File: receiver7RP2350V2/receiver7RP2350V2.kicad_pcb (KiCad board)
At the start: 4 copper layers, 46.5 x 51.8 mm, 69 parts, among them J1 BM04B-SRSS-TB, J10 S2B-PH-SM4-TB, J4 2pads, J6 MM60-52B1-E1-R650, J7 USB4105-GF-A, J8 S2B-PH-SM4-TB, U1 RP2350_60QFN, U2 USBLC6-2SC6, U3 AP7361C-33Y5-13, U4 MCP73871-2CCI_ML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

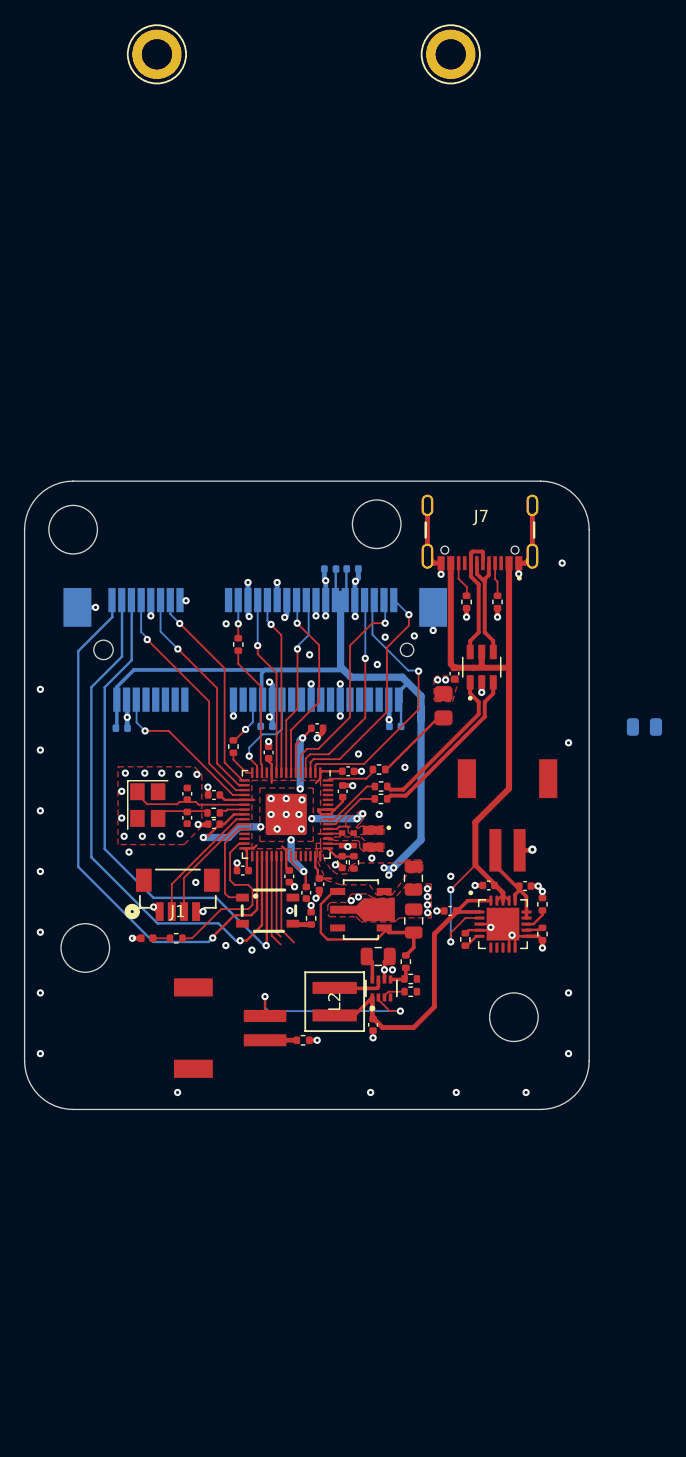
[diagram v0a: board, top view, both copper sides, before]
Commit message: add rp2350V2
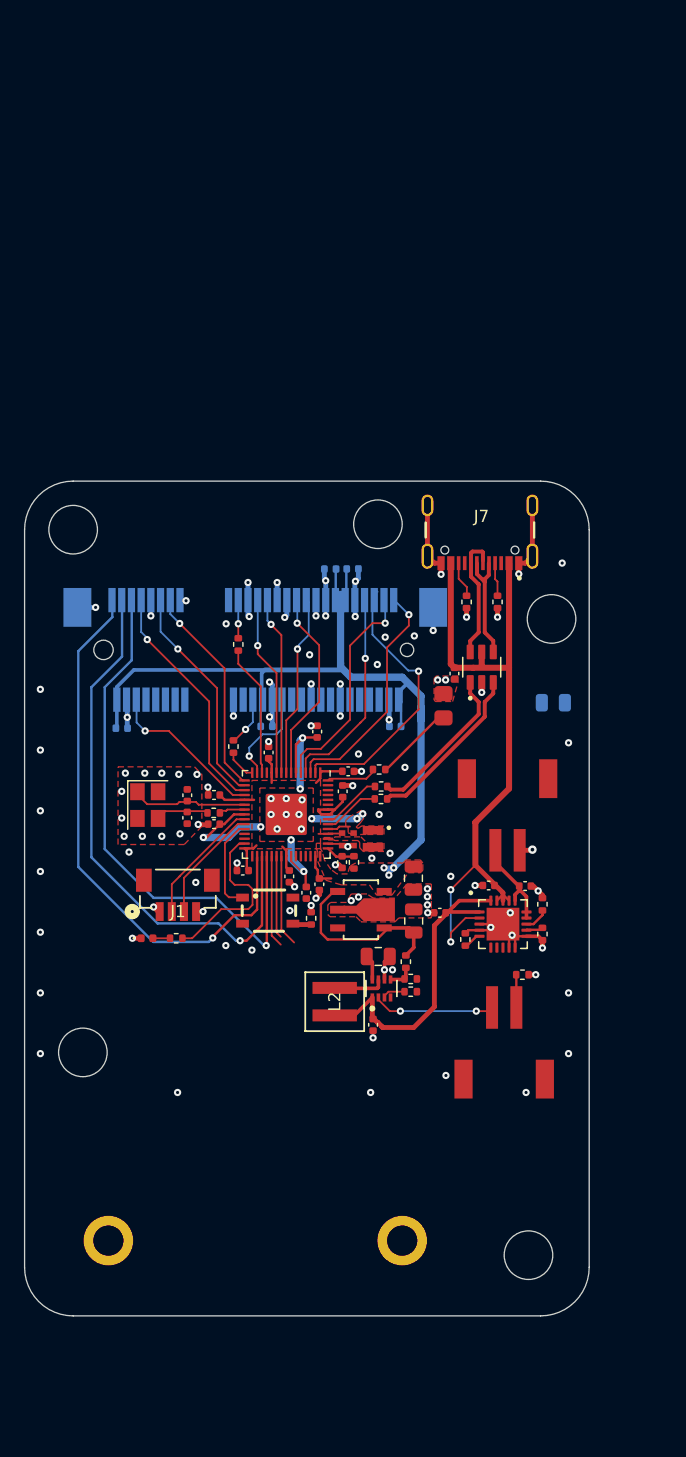
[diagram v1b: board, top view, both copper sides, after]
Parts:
- added H8: MountingHole, TF:MountingHole_4mm_t4, F.Cu at (116.6, 85.2)
- REF** (x2): moved to B.Cu
- moved REF** 101.7 mm to (94.4, 144.2), turned to 180 degrees
- moved REF** 99.8 mm to (118.6, 144.2), turned to 180 degrees
- moved J10 22.7 mm to (127.0, 128.0), turned to 0 degrees
- moved H6 19.6 mm to (129.0, 145.4)
- moved R15 18.9 mm to (128.5, 122.3)
- moved H8 16.4 mm to (130.9, 93.0)
- moved H5 8.60 mm to (92.3, 128.7)
- moved C19 7.76 mm to (131.1, 99.9)
- moved C27 0.86 mm to (121.7, 117.2)
- moved C11 0.28 mm to (111.6, 102.3), turned to 90 degrees
- moved C20 0.11 mm to (100.9, 107.5)
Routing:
- net Net-(U5-EN): track 16.4 -> 10.3 mm
- net /V_LOAD: track 25.2 -> 26.5 mm
- net GND: track 76.0 -> 75.3 mm, vias 112 -> 111
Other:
- board size 46.5 x 51.8 mm -> 46.5 x 68.8 mm

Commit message: add panelized files
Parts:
- removed C19, C29: 10u, Capacitor_SMD:C_0805_2012Metric
- removed H8 (x2): MountingHole, TF:MountingHole_4mm_t4
- removed L2: 1uH, EXLA1V0402_1RO_R:IND_EXLA-0402_EAT-L
- removed R17: 750k, Resistor_SMD:R_0402_1005Metric
- removed R18: 71.5k 1%, Resistor_SMD:R_0402_1005Metric
- removed REF** (x2): , NT4R1600:JAE_Electronics-NT4R1600-MFG
- removed U3: AP7361C-33Y5-13, AP7361C_33Y5_13:SOT89-5_DIO-M_MODGND
- added C30: 10u, Capacitor_SMD:C_0805_2012Metric, F.Cu at (129.7, 109.4)
- added D2: SMAJ6.0CA, Diode_SMD:D_SMA, F.Cu at (129.8, 102.0)
- added G***: LOGO, LOGO, F.Cu at (109.4, 141.8)
- added H1: MountingHole, MountingHole:MountingHole_2.5mm, F.Cu at (130.8, 94.1)
- added H5: MountingHole, MountingHole:MountingHole_2.7mm_M2.5_Pad_Via, F.Cu at (116.7, 85.6)
- added J2: NT4R1600, NT4R1600:JAE_Electronics-NT4R1600-MFG, B.Cu at (94.4, 144.2)
- added J3: NT4R1600, NT4R1600:JAE_Electronics-NT4R1600-MFG, B.Cu at (118.6, 144.2)
- added J5: USB4105-GF-A, USB4105_GF_A:GCT_USB4105-GF-A, F.Cu at (105.5, 83.7)
- added R19: 3.3k, Resistor_SMD:R_0402_1005Metric, F.Cu at (121.5, 113.4)
- added R20: 330k, Resistor_SMD:R_0402_1005Metric, F.Cu at (124.4, 107.3)
- C22, C23: value 10u -> 4.7u; footprint Capacitor_SMD:C_0805_2012Metric -> Capacitor_SMD:C_0402_1005Metric
- C24: moved to B.Cu
- C25: value 10u -> 100n
- C26: footprint Capacitor_SMD:C_0402_1005Metric -> Capacitor_SMD:C_0805_2012Metric
- C27, C28: value 10u -> 4.7u
- H2: renamed from H5; footprint TF:MountingHole_4mm_t4 -> MountingHole:MountingHole_2.7mm_M2.5_Pad_Via
- H3: renamed from H6; footprint TF:MountingHole_4mm_t4 -> MountingHole:MountingHole_2.7mm_M2.5_Pad_Via
- H4: renamed from H7; footprint TF:MountingHole_4mm_t4 -> MountingHole:MountingHole_2.7mm_M2.5_Pad_Via
- R12: value 3.3k -> 10k
- R14: value 24.9k -> 3.3k
- R15, R16: value 3.3k -> 5.1k
- U4: value MCP73871-2CCI_ML -> MP2664GG-0000-Z; footprint MCP73871_2CCI_ML:QFN50P400X400X100-21N -> MP2664GG-0000-Z:QFN50P200X200X105-10N
- U5: value TPS610333DRLR -> NCP186AMX330TAG; footprint TPS61033DRLR:DRL0008A-MFG_mod2 -> NCP186AMX330TAG:PSON40P160X120X45-9N
- moved R16 41.9 mm to (99.5, 86.8), turned to -90 degrees
- moved R15 39.4 mm to (111.5, 86.8), turned to 90 degrees
- moved J10 36.3 mm to (92.0, 118.2)
- moved H2 25.0 mm to (94.4, 153.6)
- moved R13 14.0 mm to (126.0, 105.5)
- moved H3 13.2 mm to (118.6, 153.6)
- moved R12 11.8 mm to (124.4, 106.2), turned to 180 degrees
- moved R14 11.6 mm to (121.0, 111.9), turned to -90 degrees
- moved C28 11.0 mm to (116.2, 115.4), turned to 180 degrees
- moved J8 9.20 mm to (127.2, 118.3), turned to 0 degrees
- moved C26 8.45 mm to (128.9, 106.5)
- moved U4 8.23 mm to (126.9, 109.9), turned to -90 degrees
- moved C27 7.53 mm to (127.5, 112.4)
- moved U5 6.63 mm to (117.5, 116.8), turned to -90 degrees
- moved C25 6.20 mm to (124.8, 108.8), turned to -90 degrees
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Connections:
- C22 pad 1: GND -> +3V3
- C22 pad 2: +3V3 -> GND
- C23 pad 1: +5V -> /V_LOAD
- C24 pad 1: VBUS -> /VPHONE
- C25 pad 1: VBUS -> /VDD
- C26 pad 1: Net-(U4-VBAT) -> /VBUS
- C27 pad 1: /V_LOAD -> /BAT_PWR
- C28 pad 1: GND -> +3V3
- C28 pad 2: /V_LOAD -> GND
- J10 pad 1: Net-(U5-EN) -> /V_LOAD
- J10 pad 2: Net-(J10-Pad2) -> /V_EN
- J7 pad A4_B9: VBUS -> /VPHONE
- J7 pad B4_A9: VBUS -> /VPHONE
- J8 pad 2: Net-(U4-VBAT) -> /BAT_PWR
- R12 pad 1: GND -> Net-(U4-NTC)
- R12 pad 2: Net-(U4-PROG1) -> /VDD
- R13 pad 2: Net-(U4-THERM) -> Net-(U4-NTC)
- R14 pad 1: GND -> /SCL0
- R14 pad 2: Net-(U4-PROG3) -> +3V3
- R15 pad 2: Net-(J10-Pad2) -> Net-(J5-CC1)
- R16 pad 1: GND -> Net-(J5-CC2)
- R16 pad 2: Net-(U5-MODE) -> GND
- S1 pad 3: Net-(R1-Pad2) -> unconnected-(S1-Pad3)
- U1 pad 35: /GPIO23 -> /INT_BAT
- U1 pad 36: unconnected-(U1-GPIO24-Pad36) -> /SDA0
- U1 pad 37: unconnected-(U1-GPIO25-Pad37) -> /SCL0
- U2 pad 5: VBUS -> /VPHONE
- U4 pad 1: /V_LOAD -> /VBUS
- U4 pad 10: GND -> /V_LOAD
- U4 pad 2: VBUS -> Net-(U4-NTC)
- U4 pad 3: GND -> /INT_BAT
- U4 pad 4: GND -> /VDD
- U4 pad 5: Net-(U4-THERM) -> GND
- U4 pad 6: unconnected-(U4-~{PG}-Pad6) -> /SCL0
- U4 pad 7: unconnected-(U4-STAT2-Pad7) -> /SDA0
- U4 pad 8: unconnected-(U4-STAT1/*LBO-Pad8) -> /BAT_PWR
- U4 pad 9: GND -> /BAT_PWR
- U5 pad 1: /V_LOAD -> +3V3
- U5 pad 2: Net-(U5-EN) -> +3V3
- U5 pad 3: Net-(U5-MODE) -> GND
- U5 pad 4: unconnected-(U5-PG-Pad4) -> +3V3
- U5 pad 5: Net-(U5-FB) -> GND
- U5 pad 6: GND -> /V_EN
- U5 pad 7: Net-(U5-SW) -> /V_LOAD
- U5 pad 8: +5V -> /V_LOAD
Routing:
- net VBUS: track 57.0 -> 0.00 mm, vias 2 -> 0
- net /VBUS: track 0.00 -> 43.8 mm
- net /INT_BAT: track 0.00 -> 42.2 mm, vias 0 -> 2
- net /V_EN: track 0.00 -> 35.7 mm
- net /SDA0: track 0.00 -> 33.8 mm, vias 0 -> 2
- net /V_LOAD: track 26.5 -> 59.9 mm
- net /SCL0: track 0.00 -> 32.4 mm, vias 0 -> 2
- net /VPHONE: track 0.00 -> 20.6 mm, vias 0 -> 2
- net +5V: track 17.4 -> 0.00 mm
- net GND: track 75.3 -> 60.1 mm, vias 111 -> 180
- net Net-(U5-EN): track 10.3 -> 0.00 mm, vias 2 -> 0
- net Net-(U4-VBAT): track 7.68 -> 0.00 mm
- net /GPIO23: track 7.60 -> 0.00 mm
- net unconnected-(U1-GPIO25-Pad37): track 7.55 -> 0.00 mm
- net unconnected-(U1-GPIO24-Pad36): track 6.78 -> 0.00 mm
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- added copper zone on F.Cu, net /BAT_PWR
- added copper zone on F.Cu, net /VBUS
- added copper zone on F.Cu, net /VDD
- added copper zone on F.Cu, net /V_LOAD
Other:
- board size 46.5 x 68.8 mm -> 46.5 x 78.3 mm
- rule pad_to_mask_clearance: 0.0508 -> 0

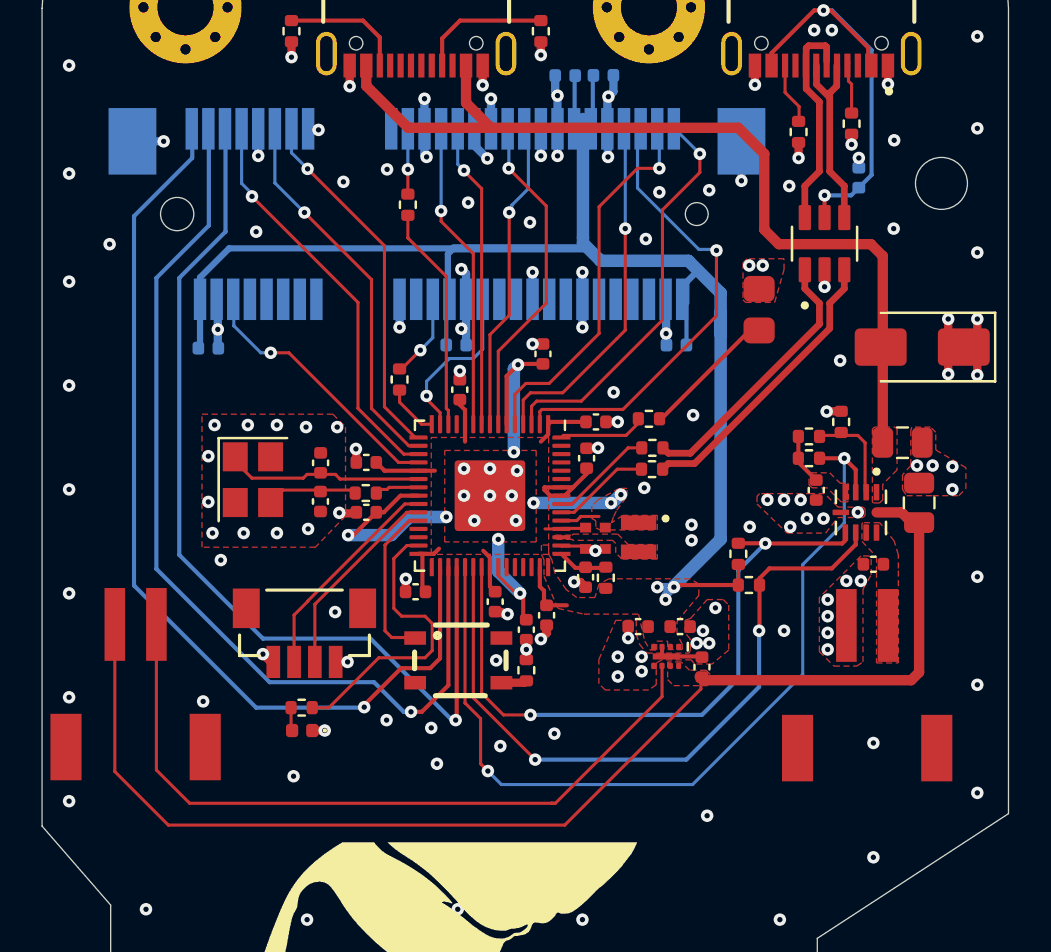
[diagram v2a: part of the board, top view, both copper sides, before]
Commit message: updates to receiver layout
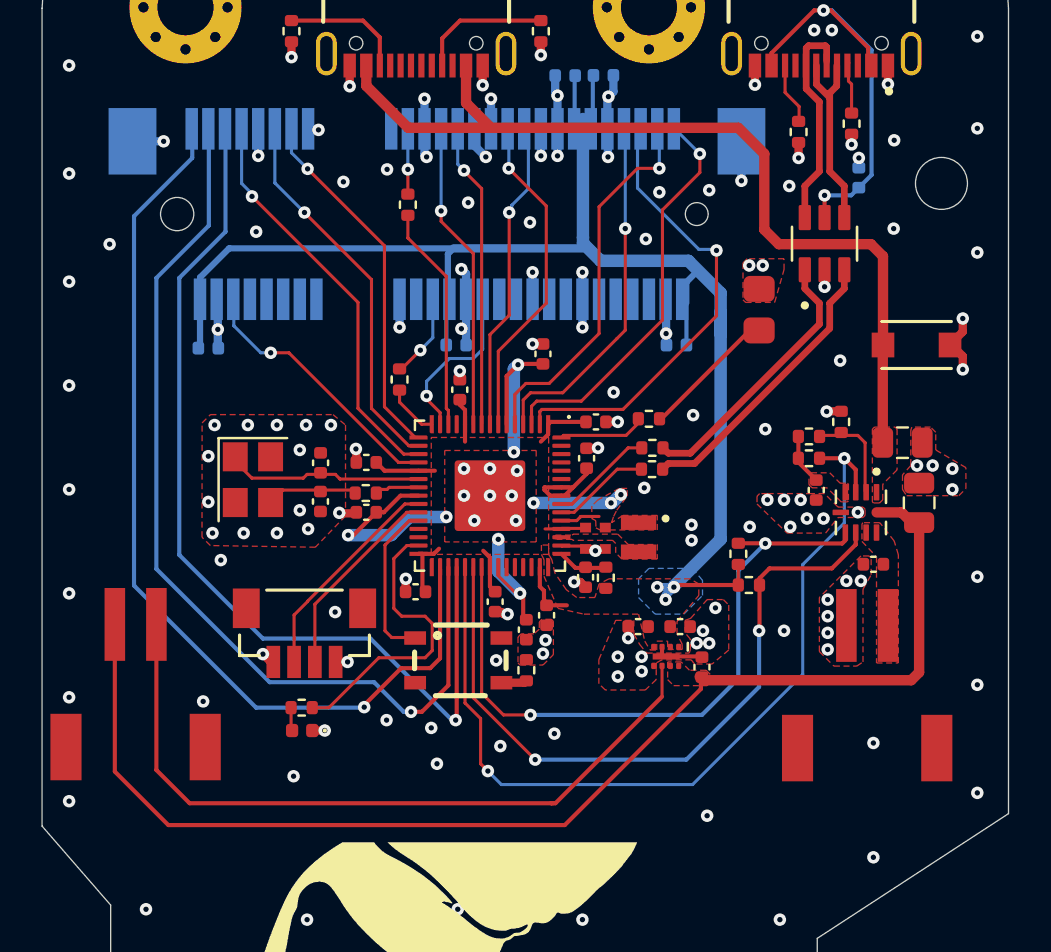
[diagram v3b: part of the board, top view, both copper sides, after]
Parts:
- D2: value SMAJ6.0CA -> SMF6.0CA; footprint Diode_SMD:D_SMA -> SMF26CA_custom:SMF26CA_Custom
- U1: value RP2350_60QFN -> RP2354_60QFN
- moved D2 0.29 mm to (129.6, 101.8)
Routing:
- net GND: track 60.1 -> 57.2 mm, vias 180 -> 181
- added copper zone on B.Cu, net +3V3

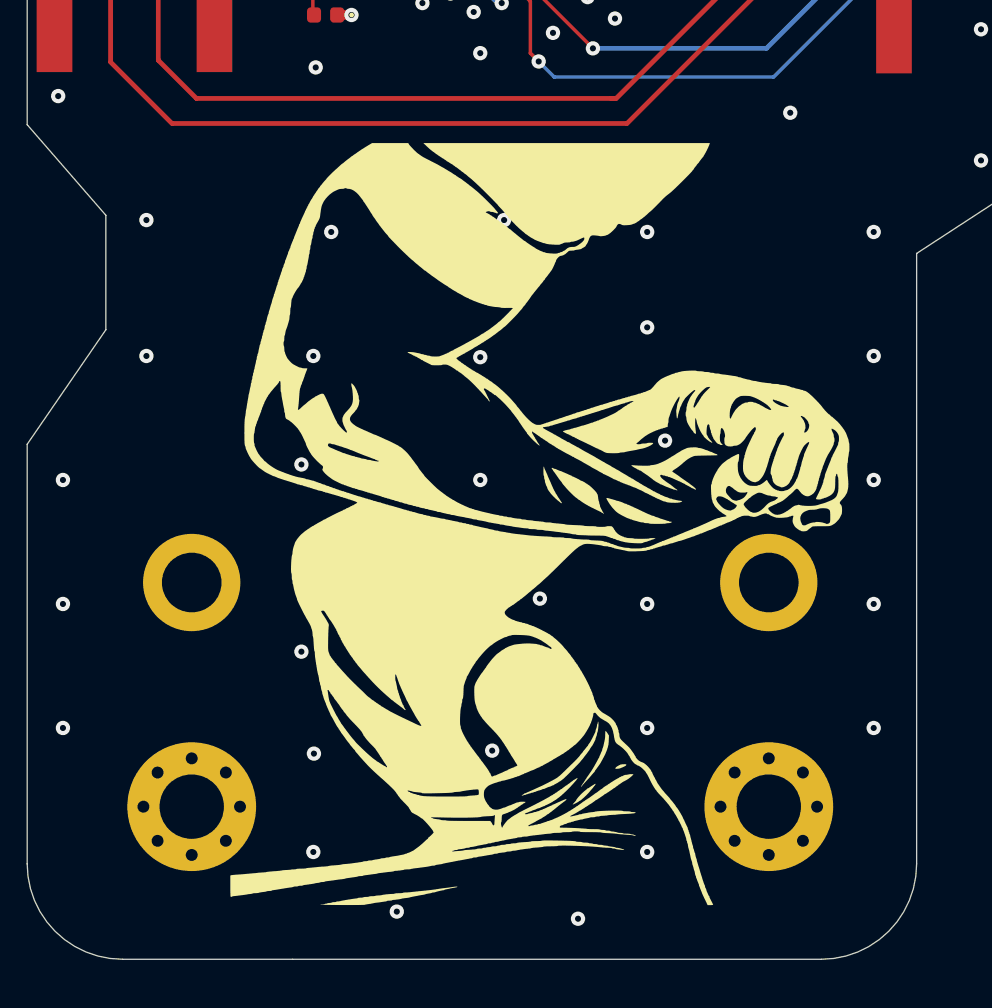
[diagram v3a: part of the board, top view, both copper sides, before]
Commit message: add pdf of design and changes to board
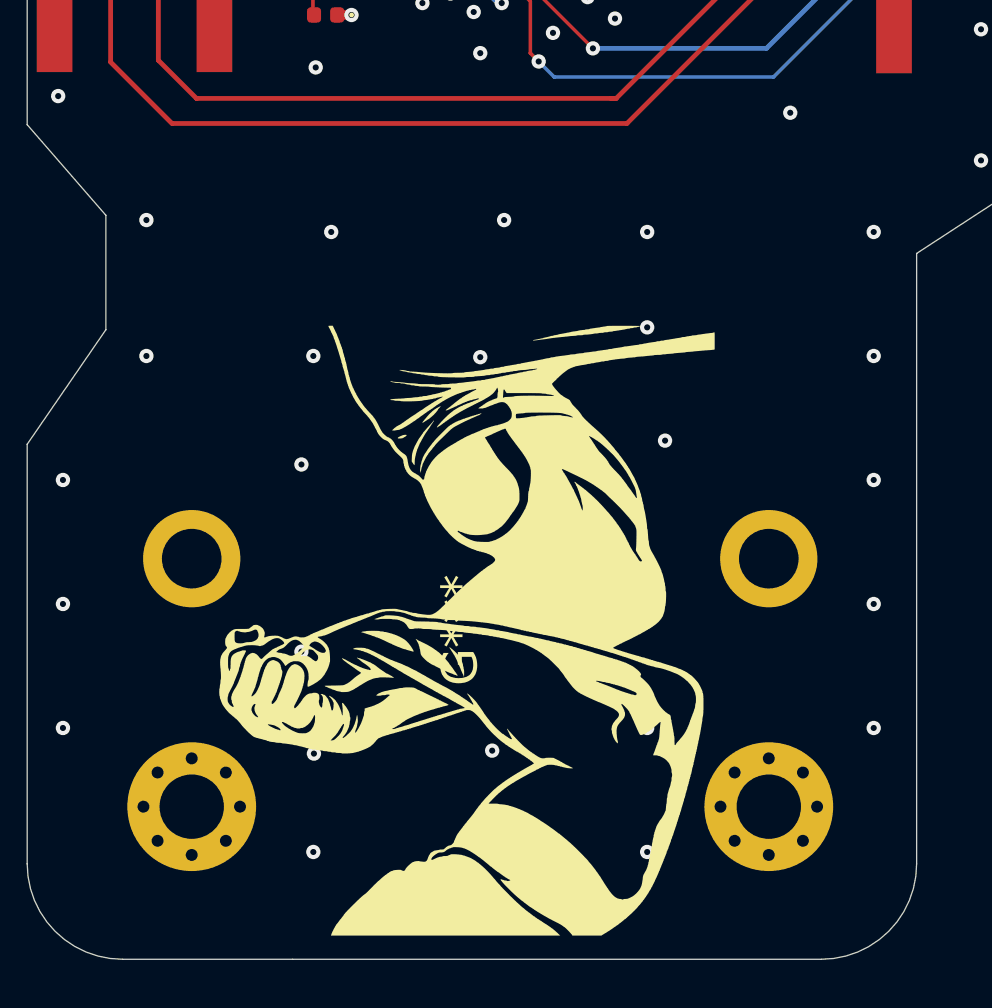
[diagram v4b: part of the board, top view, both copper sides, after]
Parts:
- moved G*** 5.78 mm to (105.7, 146.2), turned to 90 degrees
- moved J2 1.00 mm to (94.4, 143.2)
- moved J3 1.00 mm to (118.6, 143.2)
